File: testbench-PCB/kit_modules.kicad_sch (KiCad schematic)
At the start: 12 parts, among them U2 Rotary_encoder_switch_module, U3 Thermistor_module, U4 Relay_module, U6 Matrix_keyboard, U7 RTC_EEPROM_module, U8 LCD_display

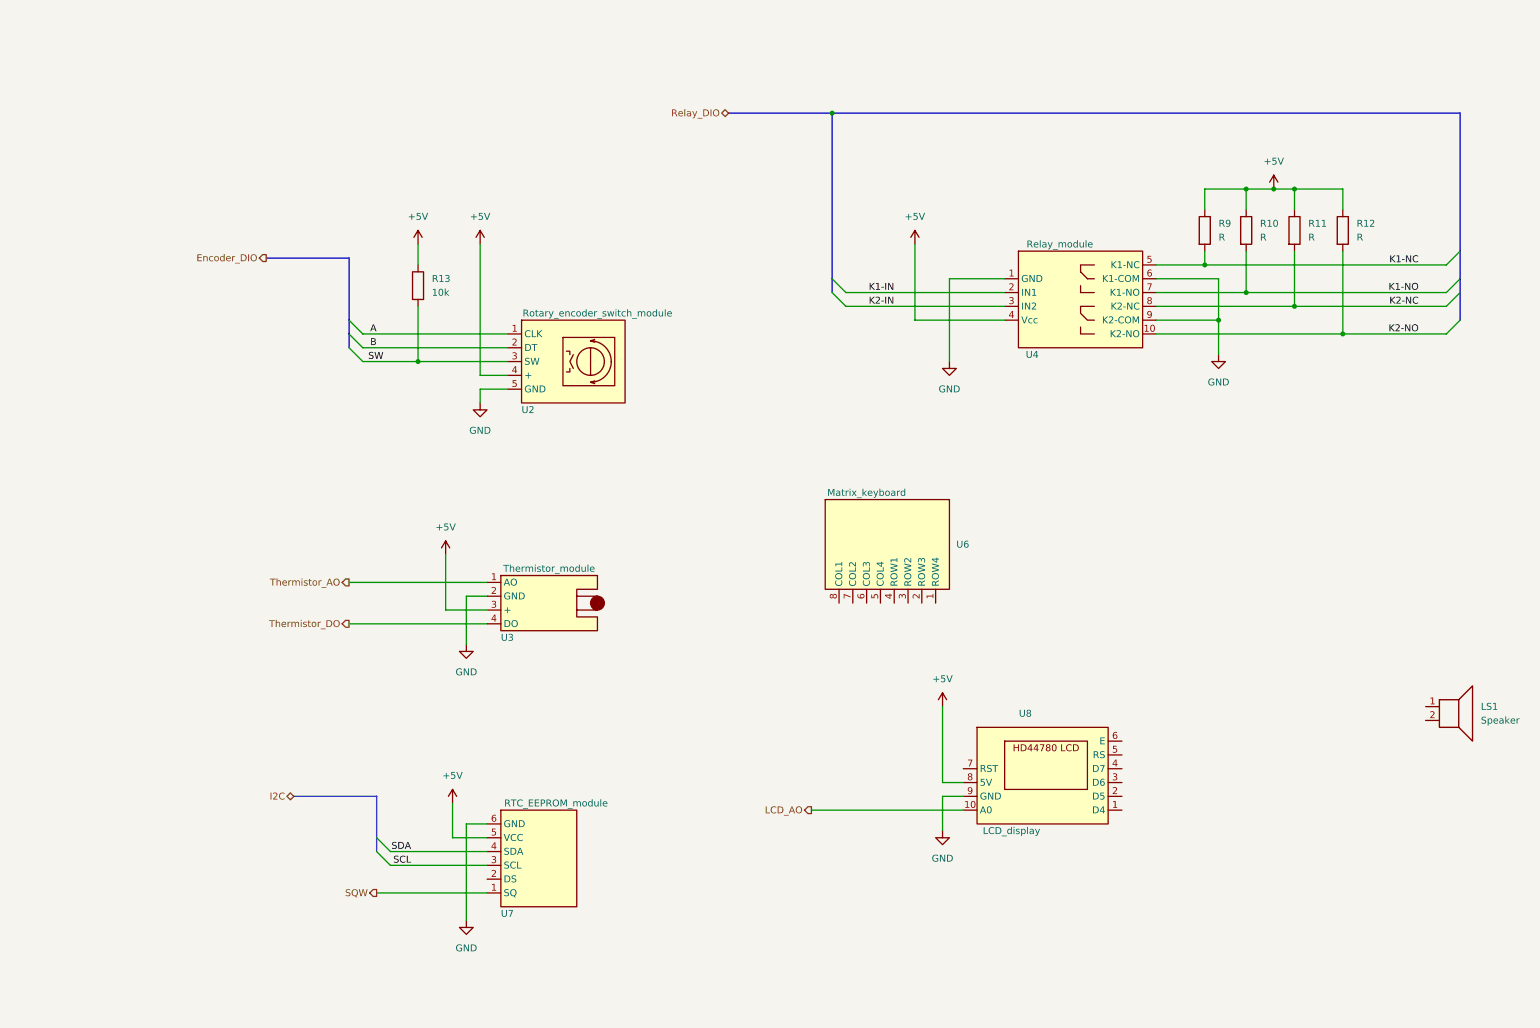
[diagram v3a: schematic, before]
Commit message: Finished connection between modules and MCU.
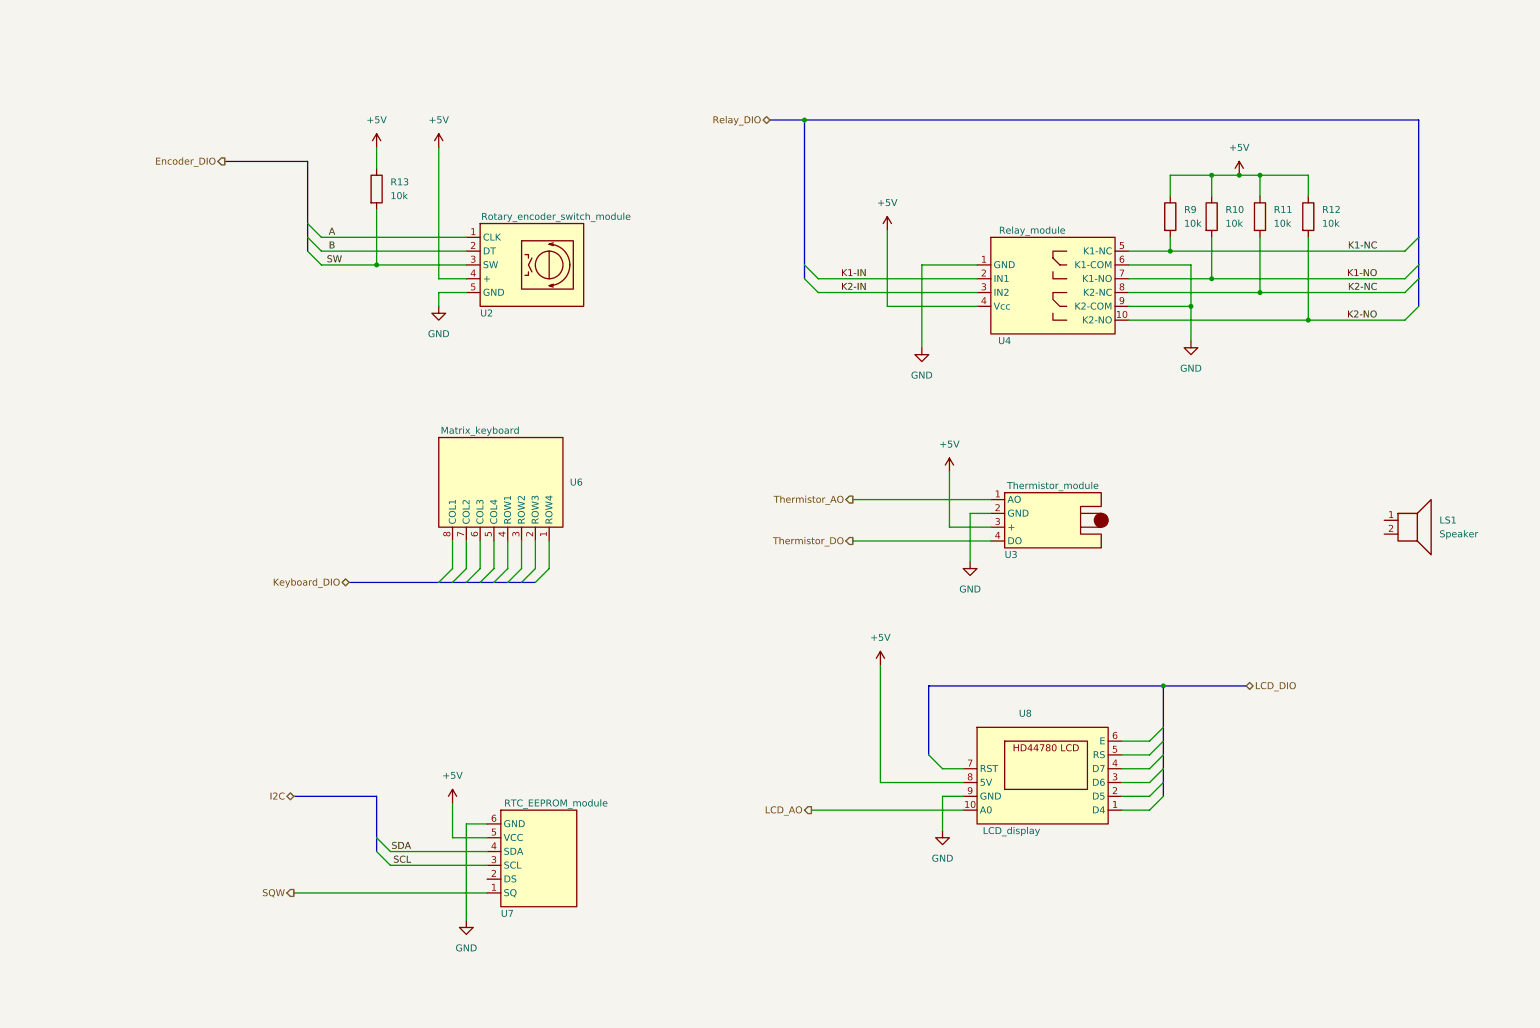
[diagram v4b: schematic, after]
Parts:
- R10, R11, R12, R9: value R -> 10k
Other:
- moved on the sheet: LS1, R10, R11, R12, R13, R9, U2, U3, U4, U6

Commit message: Added footprints to few parts.
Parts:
- U2: footprint (none) -> Connector_PinSocket_2.54mm:PinSocket_1x05_P2.54mm_Horizontal
- U3: footprint (none) -> Connector_PinSocket_2.54mm:PinSocket_1x04_P2.54mm_Horizontal
- U6: footprint (none) -> Connector_PinSocket_2.54mm:PinSocket_1x08_P2.54mm_Vertical
- U7: footprint (none) -> Connector_PinSocket_2.54mm:PinSocket_1x06_P2.54mm_Horizontal
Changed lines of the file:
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@@
       (effects (font (size 1.27 1.27)))
     )
-    (property "Footprint" "" (at 78.74 95.25 0)
+    (property "Footprint" "Connector_PinSocket_2.54mm:PinSocket_1x08_P2.54mm_Vertical" (at 78.74 95.25 0)
       (effects (font (size 1.27 1.27)) hide)
     )
@@
       (effects (font (size 1.27 1.27)))
     )
-    (property "Footprint" "" (at 180.34 93.98 0)
+    (property "Footprint" "Connector_PinSocket_2.54mm:PinSocket_1x04_P2.54mm_Horizontal" (at 180.34 93.98 0)
       (effects (font (size 1.27 1.27)) hide)
     )
@@
       (effects (font (size 1.27 1.27)))
     )
-    (property "Footprint" "" (at 87.63 50.8 0)
+    (property "Footprint" "Connector_PinSocket_2.54mm:PinSocket_1x05_P2.54mm_Horizontal" (at 87.63 50.8 0)
       (effects (font (size 1.27 1.27)) hide)
     )
@@
       (effects (font (size 1.27 1.27)))
     )
-    (property "Footprint" "" (at 91.44 166.37 0)
-      (effects (font (size 1.27 1.27)) hide)
-    )
+    (property "Footprint" "Connector_PinSocket_2.54mm:PinSocket_1x06_P2.54mm_Horizontal" (at 91.44 166.37 0)
+      (effects (font (size 1.27 1.27)) hide)
+    )

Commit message: Changed naming convention.
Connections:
- net SCL renamed I2C_SCL
- net SDA renamed I2C_SDA
- net SQW renamed RTC_SQW
- no-connect marks 0 -> 1
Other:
- note added: "KEY_D[0..7]"
- moved on the sheet: U6

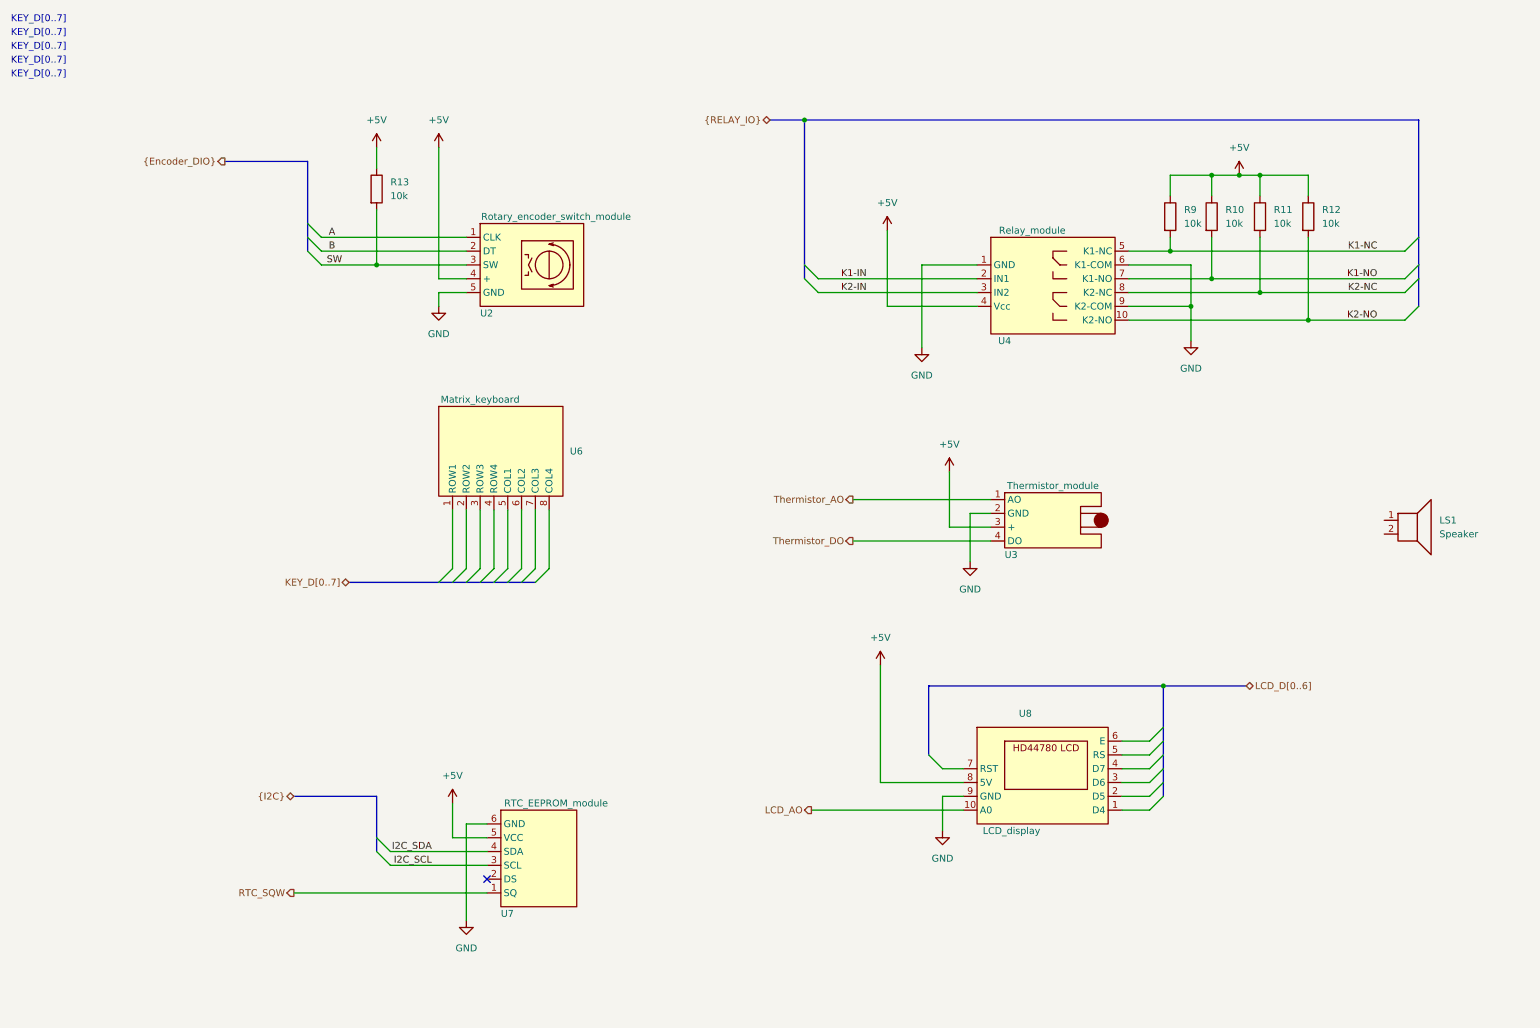
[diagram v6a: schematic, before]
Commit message: Connecter speaker, added JTAG.
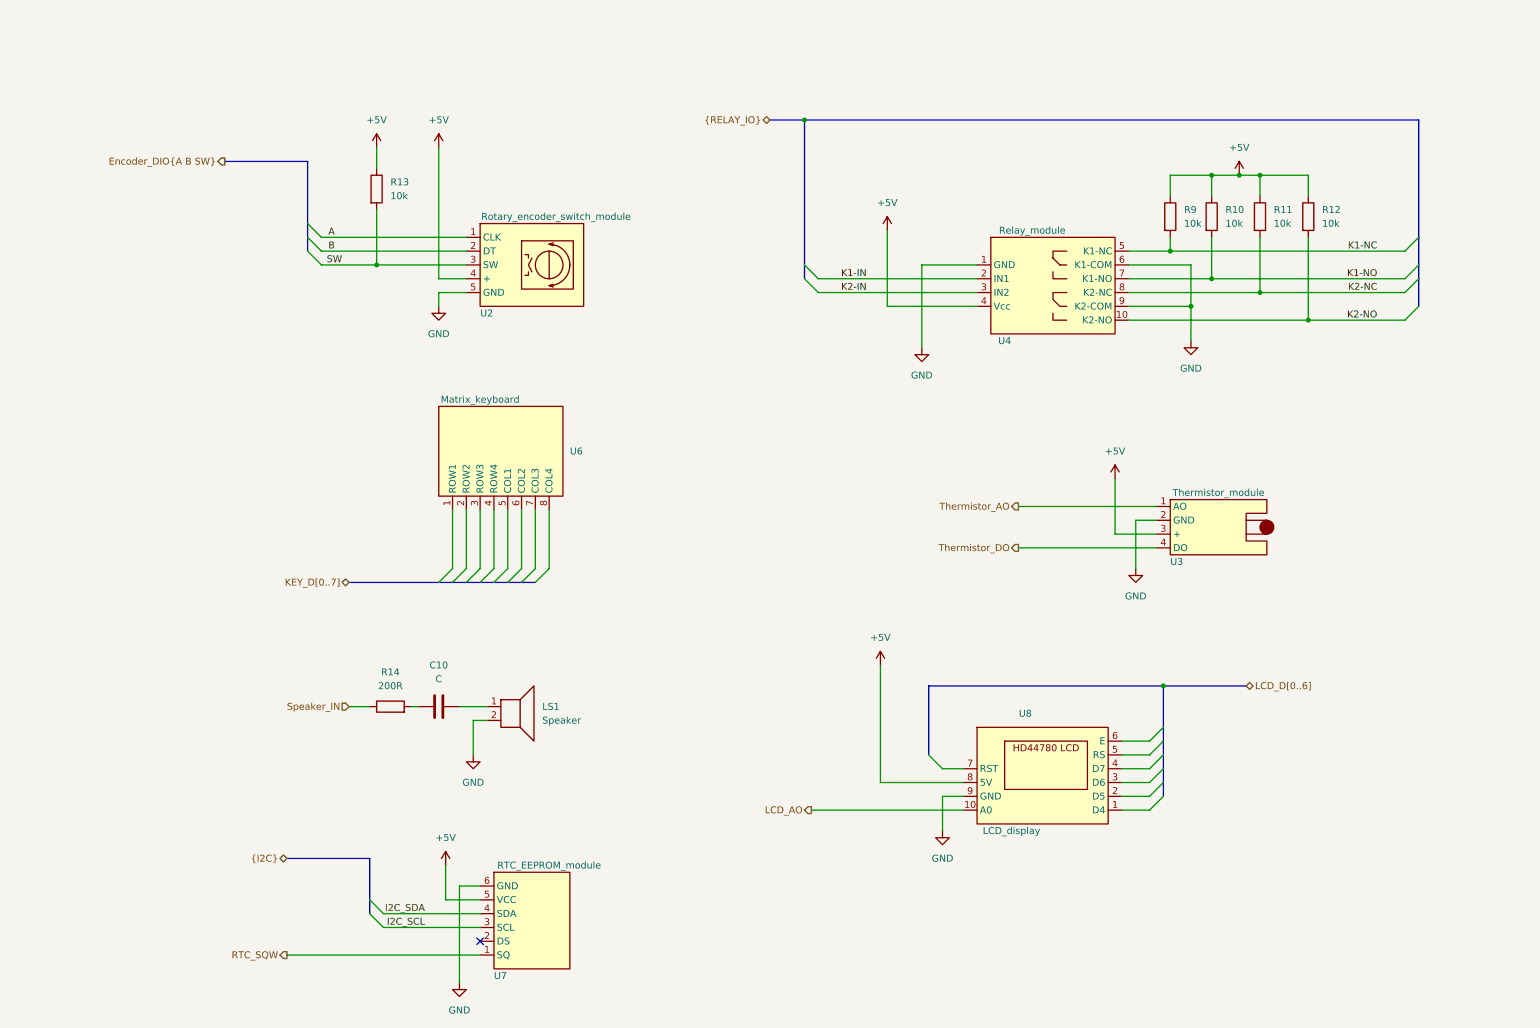
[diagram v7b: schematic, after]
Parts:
- added C10: C, symbol Device:C
- added R14: 200R, Resistor_SMD:R_0805_2012Metric, symbol Device:R
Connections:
- net GND: now also LS1.2
- net at LS1.1: now also C10.2
- new net: C10.1, R14.2
- new net Speaker_IN: R14.1
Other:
- note removed: "KEY_D[0..7]"
- moved on the sheet: LS1, U3, U7

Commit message: Created PCB, changed footprints for symbols.
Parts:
- LS1: footprint (none) -> Connector_PinHeader_2.54mm:PinHeader_1x02_P2.54mm_Vertical
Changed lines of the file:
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@@
       (effects (font (size 1.27 1.27)) (justify left))
     )
-    (property "Footprint" "" (at 92.71 133.35 0)
+    (property "Footprint" "Connector_PinHeader_2.54mm:PinHeader_1x02_P2.54mm_Vertical" (at 92.71 133.35 0)
       (effects (font (size 1.27 1.27)) hide)
     )
